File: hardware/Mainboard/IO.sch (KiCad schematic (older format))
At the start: 14 parts, among them SW2 INTERRUPT, SW3 PORT B, SW5 CARRIER, X3 EXPANSION

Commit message: Misc: 	- Update README 	- Add 74HC138 datasheet 	- Update board image 	- Add layout for website tutorial
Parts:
- removed RN1: 10k, Resistor_THT:R_Array_SIP11, symbol Device:R_Network10
- added X8: PORT B, Connector_PinHeader_2.54mm:PinHeader_1x10_P2.54mm_Vertical, symbol Connector_Generic:Conn_01x10
- X1: renamed from X3; Mfr. Harwin -> TE Connectivity / AMP; Mfr. No. M20-9742046 -> 4-103328-5; Mouser 855-M20-9742046 -> 571-4-103328-5
- renumbered D0 to D1, D1 to D2, D2 to D3, D3 to D4, D4 to D5, D5 to D6, D6 to D7, D7 to D8, RN2 to RN1, SW5 to SW1, SW3 to SW2, SW2 to SW3
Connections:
- net CB0 is gone; now on net CB1: SW3.2
- net +5V: no longer SW2.10, SW2.11, SW2.12, SW2.13, SW2.14, SW2.15, SW2.16, SW2.9, SW3.3, SW3.4
- net CB1: now also X8.2 (Pin_2); no longer SW3.1
- net GND: now also SW2.10, SW2.11, SW2.12, SW2.13, SW2.14, SW2.15, SW2.16, SW2.9, SW3.3, SW3.4
- net PB0: now also X8.10 (Pin_10)
- net PB1: now also X8.9 (Pin_9)
- net PB2: now also X8.8 (Pin_8)
- net PB3: now also X8.7 (Pin_7)
- net PB4: now also X8.6 (Pin_6)
- net PB5: now also X8.5 (Pin_5)
- net PB6: now also X8.4 (Pin_4)
- net PB7: now also X8.3 (Pin_3)
- new net CB2: SW3.1, X8.1 (Pin_1)
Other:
- note added: "NOTE: The I/O lines of W65C22N have \ninternal current limiting resistors."
- moved on the sheet: SW2, SW3

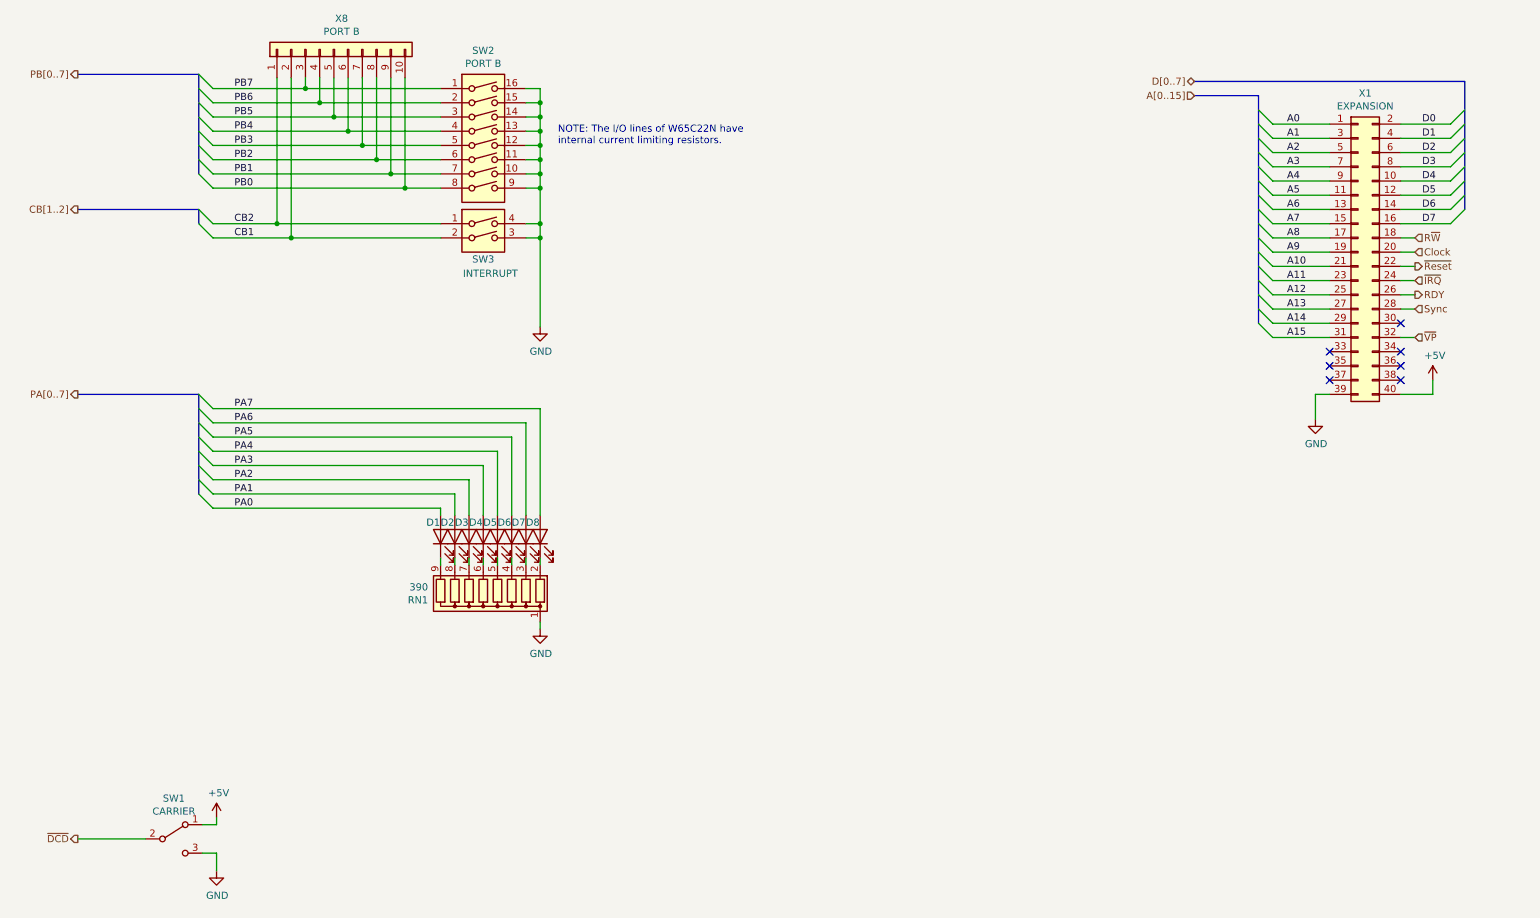
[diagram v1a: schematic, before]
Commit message: Hardware: 	- Add pull up resistor for PB
Documentation:
	- Add more datasheets
	- Update documentation

Misc:
	- Rename CHANGELOG
	- Remove old files

Signed-off-by: Daniel Kampert <DanielKampert@kampis-elektroecke.de>
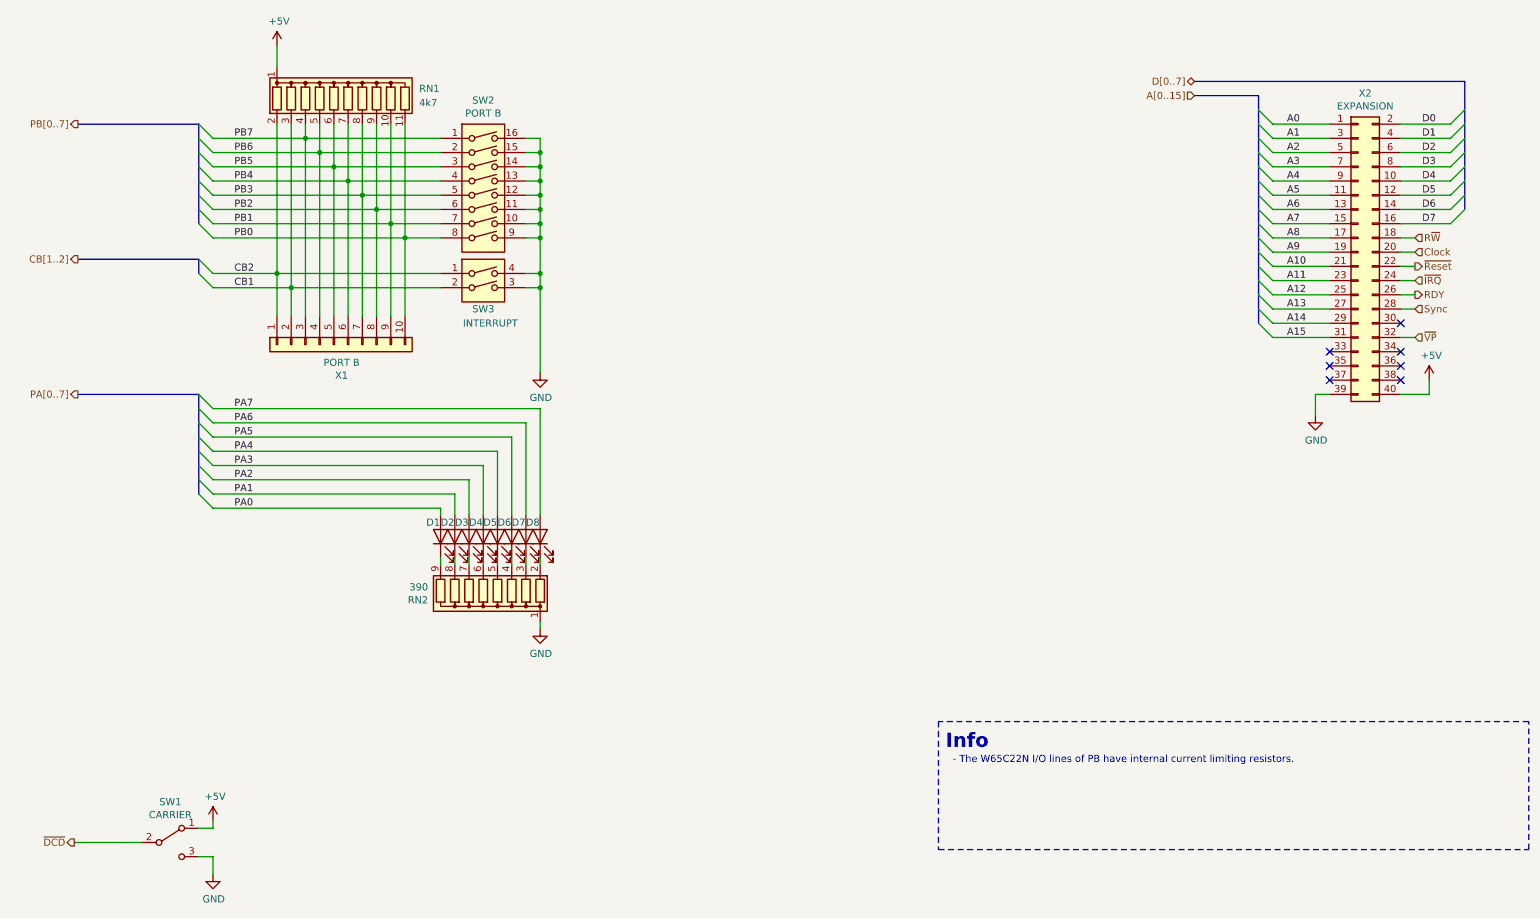
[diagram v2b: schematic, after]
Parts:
- added RN1: 4k7, Resistor_THT:R_Array_SIP11, symbol Device:R_Network10
- D1, D2, D3, D4, D5, D6, D7, D8: Distributor (none) -> Mouser; Order Number (none) -> 941-C503BRANCZ0C0AA1
- RN2: renamed from RN1; Distributor (none) -> Mouser; Order Number (none) -> 652-4609X-1LF-390
- SW1: Distributor (none) -> Mouser; Order Number (none) -> 612-EG1224
- SW2: Distributor (none) -> Mouser; Order Number (none) -> 113-NDI08SV
- SW3: Distributor (none) -> Mouser; Order Number (none) -> 113-NDI02SV
- X1: renamed from X8; Distributor (none) -> Mouser; Order Number (none) -> 571-1-825433-0
- X2: renamed from X1; Distributor (none) -> Mouser; Order Number (none) -> 571-4-103328-5
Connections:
- net +5V: now also RN1.1 (common)
- net CB1: now also RN1.3 (R2)
- net CB2: now also RN1.2 (R1)
- net PB0: now also RN1.11 (R10)
- net PB1: now also RN1.10 (R9)
- net PB2: now also RN1.9 (R8)
- net PB3: now also RN1.8 (R7)
- net PB4: now also RN1.7 (R6)
- net PB5: now also RN1.6 (R5)
- net PB6: now also RN1.5 (R4)
- net PB7: now also RN1.4 (R3)
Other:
- note added: "- The W65C22N I/O lines of PB have internal current limiting resistors."
- note added: "Info"
- note removed: "NOTE: The I/O lines of W65C22N have \ninternal current limiting resistors."
- moved on the sheet: SW1, SW2, SW3, X1
